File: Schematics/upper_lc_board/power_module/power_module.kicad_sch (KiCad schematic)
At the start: 21 parts, among them U13 ID_LM66100DCKR, U14 ID_LM66100DCKR

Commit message: finish adding components to layout, revise layout next.
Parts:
- C?: value 10uF_16V -> 22uF_16V
- C?: value 47uF_63V -> 100uF_50V
- C?: value 10uF_12V -> 22uF_12V
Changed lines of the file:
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@@
 			)
 		)
-		(property "Value" "10uF_16V"
+		(property "Value" "22uF_16V"
 			(at 57.15 143.5099 0)
 			(effects
@@
 			)
 		)
-		(property "Value" "47uF_63V"
+		(property "Value" "100uF_50V"
 			(at 57.15 167.6399 0)
 			(effects
@@
 			)
 		)
-		(property "Value" "10uF_12V"
+		(property "Value" "22uF_12V"
 			(at 57.15 120.6499 0)
 			(effects

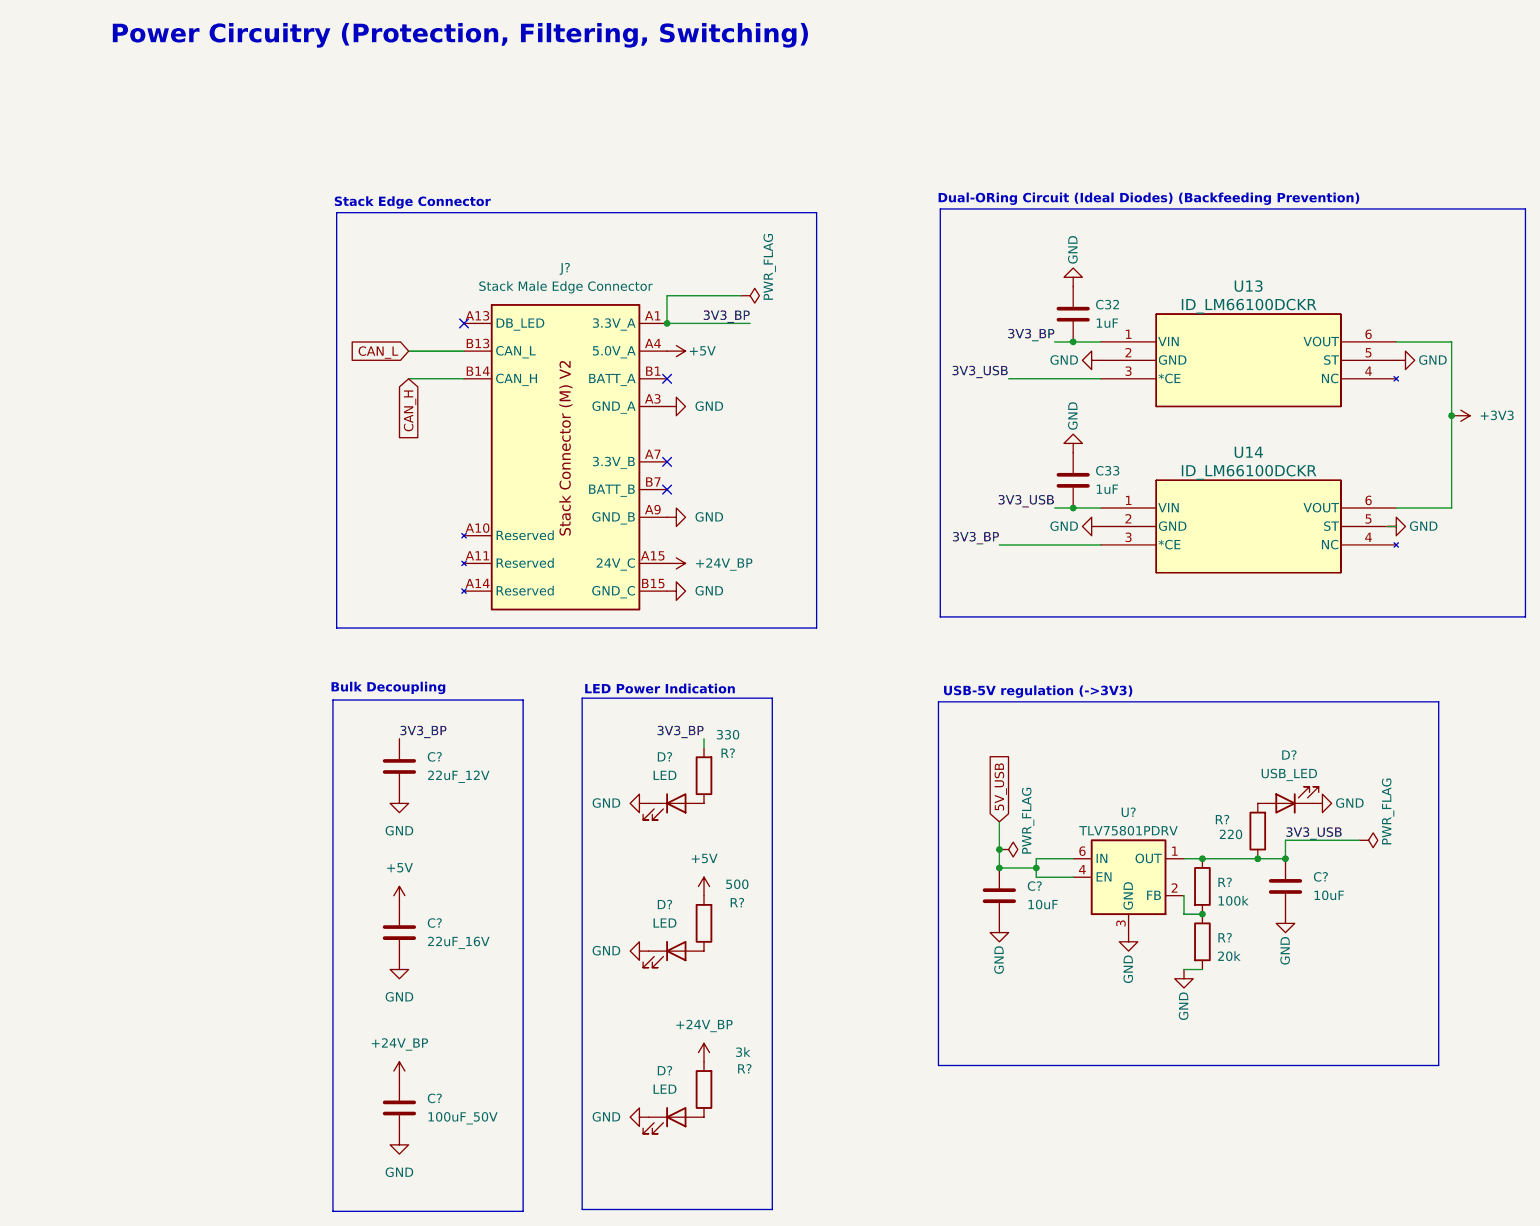
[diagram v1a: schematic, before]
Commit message: add testing points throughout board schematic
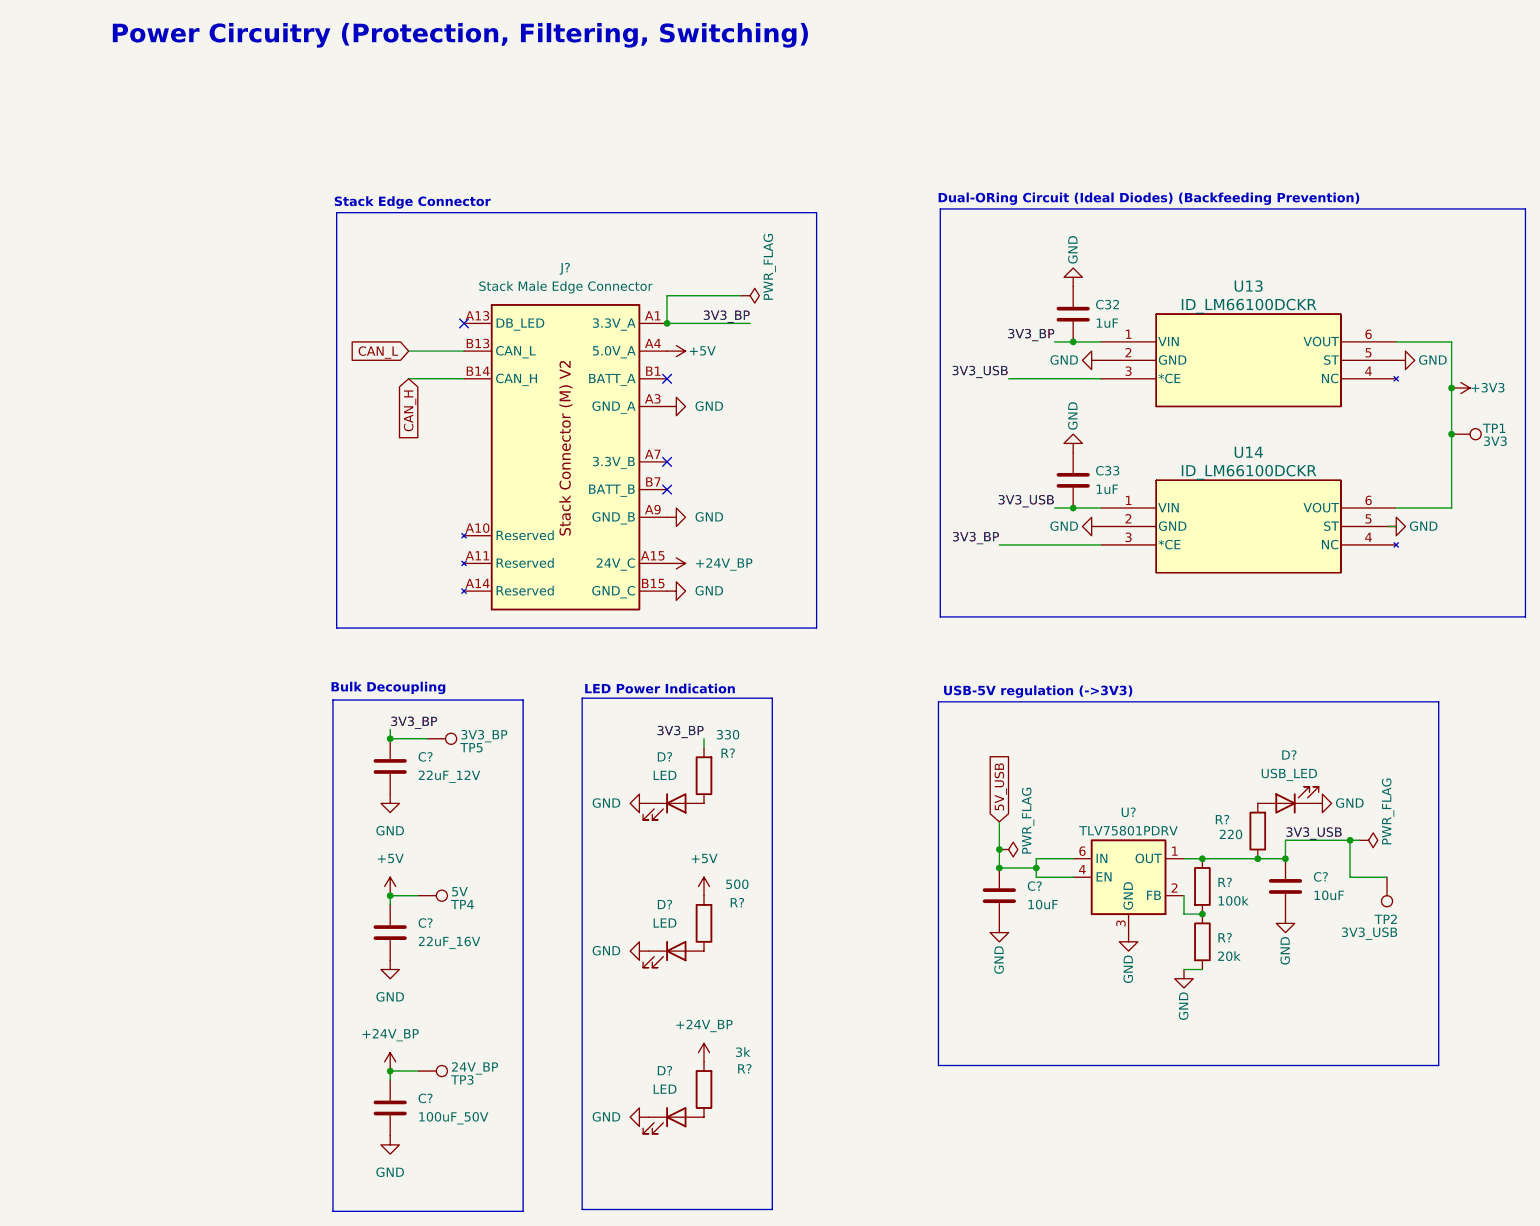
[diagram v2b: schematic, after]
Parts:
- added TP1: 3V3, TestPoint:TestPoint_Pad_1.0x1.0mm, symbol Connector:TestPoint
- added TP2: 3V3_USB, TestPoint:TestPoint_Pad_1.0x1.0mm, symbol Connector:TestPoint
- added TP3: 24V_BP, TestPoint:TestPoint_Pad_1.0x1.0mm, symbol Connector:TestPoint
- added TP4: 5V, TestPoint:TestPoint_Pad_1.0x1.0mm, symbol Connector:TestPoint
- added TP5: 3V3_BP, TestPoint:TestPoint_Pad_1.0x1.0mm, symbol Connector:TestPoint
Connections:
- net +24V_BP: now also TP3.1
- net +3V3: now also TP1.1
- net +5V: now also TP4.1
- net 3V3_BP: now also TP5.1
- net 3V3_USB: now also TP2.1
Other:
- moved on the sheet: C?

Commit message: fix shunt resistor, add test point to layout
- sync issue with backplane connector footprint
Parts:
- TP1, TP2, TP3, TP4, TP5: footprint TestPoint:TestPoint_Pad_1.0x1.0mm -> TestPoint:TestPoint_Pad_D1.0mm
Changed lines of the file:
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@@
 			)
 		)
-		(property "Footprint" "TestPoint:TestPoint_Pad_1.0x1.0mm"
+		(property "Footprint" "TestPoint:TestPoint_Pad_D1.0mm"
 			(at 184.15 134.62 0)
 			(effects
@@
 			)
 		)
-		(property "Footprint" "TestPoint:TestPoint_Pad_1.0x1.0mm"
+		(property "Footprint" "TestPoint:TestPoint_Pad_D1.0mm"
 			(at 57.15 120.65 0)
 			(effects
@@
 			)
 		)
-		(property "Footprint" "TestPoint:TestPoint_Pad_1.0x1.0mm"
+		(property "Footprint" "TestPoint:TestPoint_Pad_D1.0mm"
 			(at 198.12 78.74 0)
 			(effects
@@
 			)
 		)
-		(property "Footprint" "TestPoint:TestPoint_Pad_1.0x1.0mm"
+		(property "Footprint" "TestPoint:TestPoint_Pad_D1.0mm"
 			(at 55.88 142.24 0)
 			(effects
@@
 			)
 		)
-		(property "Footprint" "TestPoint:TestPoint_Pad_1.0x1.0mm"
+		(property "Footprint" "TestPoint:TestPoint_Pad_D1.0mm"
 			(at 55.88 166.37 0)
 			(effects

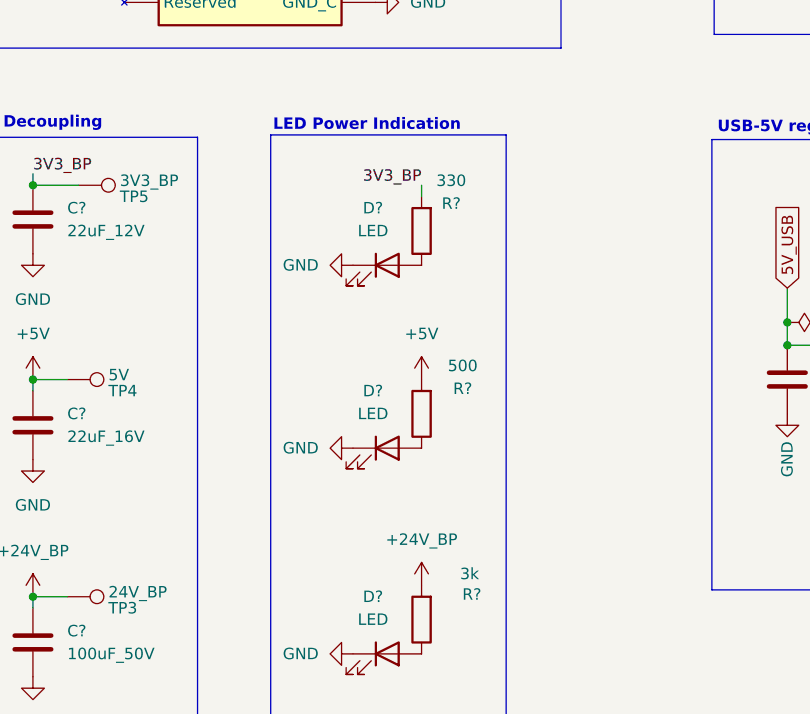
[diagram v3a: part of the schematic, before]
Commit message: start routing
- routing done for solenoids, power, and some other sub-circuits.
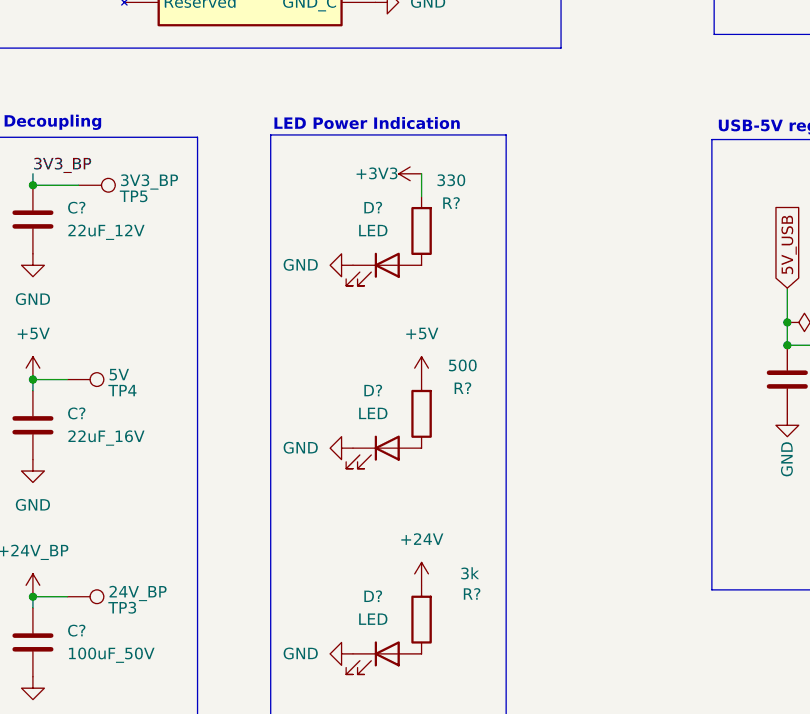
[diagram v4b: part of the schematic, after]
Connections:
- net +24V_BP: no longer R?.2
- net +3V3: now also R?.2
- net 3V3_BP: no longer R?.2
- new net +24V: R?.2
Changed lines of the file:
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@@
 	(wire
 		(pts
-			(xy 95.25 115.57) (xy 95.25 116.84)
-		)
-		(stroke
-			(width 0)
-			(type default)
-			(color 194 0 0 1)
-		)
-	)
-	(wire
-		(pts
 			(xy 143.51 83.82) (xy 146.05 83.82)
 		)
@@
 		)
 	)
+	(wire
+		(pts
+			(xy 95.25 114.3) (xy 95.25 116.84)
+		)
+		(stroke
+			(width 0)
+			(type default)
+			(color 132 0 0 1)
+		)
+	)
 	(rectangle
 		(start 44.704 43.18)
@@
 		)
 	)
-	(label "3V3_BP"
-		(at 95.25 115.57 180)
-		(fields_autoplaced yes)
-		(effects
-			(font
-				(size 1.27 1.27)
-			)
-			(justify right bottom)
-		)
-	)
 	(label "3V3_USB"
 		(at 175.26 129.54 0)
@@
 	)
 	(symbol
-		(lib_id "power:+24V")
-		(at 95.25 160.02 0)
-		(unit 1)
-		(exclude_from_sim no)
-		(in_bom yes)
-		(on_board yes)
-		(dnp no)
-		(fields_autoplaced yes)
-		(property "Reference" "#PWR?"
-			(at 95.25 163.83 0)
-			(effects
-				(font
-					(size 1.27 1.27)
-				)
-				(hide yes)
-			)
-		)
-		(property "Value" "+24V_BP"
-			(at 95.25 154.94 0)
-			(effects
-				(font
-					(size 1.27 1.27)
-				)
-			)
-		)
-		(property "Footprint" ""
-			(at 95.25 160.02 0)
-			(effects
-				(font
-					(size 1.27 1.27)
-				)
-				(hide yes)
-			)
-		)
-		(property "Datasheet" ""
-			(at 95.25 160.02 0)
-			(effects
-				(font
-					(size 1.27 1.27)
-				)
-				(hide yes)
-			)
-		)
-		(property "Description" "Power symbol creates a global label with name \"+24V\""
-			(at 95.25 160.02 0)
-			(effects
-				(font
-					(size 1.27 1.27)
-				)
-				(hide yes)
-			)
-		)
-		(pin "1"
-		)
-		(instances
-			(project "power_module"
-				(path "/056a409d-68dc-4414-8eb2-1cb0ecc0d837"
-					(reference "#PWR?")
-					(unit 1)
-				)
-			)
-			(project "power_module"
-				(path "/9b1a1d2a-fad7-4f10-83f3-1f83e9656c75/4448a9b0-3cba-4e30-89c0-980036e20f76"
-					(reference "#PWR039")
-					(unit 1)
-				)
-			)
-		)
-	)
-	(symbol
 		(lib_id "QRET_Buck_PSU:LM66100DCKR")
 		(at 170.18 63.5 0)
@@
 	)
 	(symbol
+		(lib_id "power:+3V3")
+		(at 95.25 114.3 90)
+		(unit 1)
+		(exclude_from_sim no)
+		(in_bom yes)
+		(on_board yes)
+		(dnp no)
+		(property "Reference" "#PWR041"
+			(at 99.06 114.3 0)
+			(effects
+				(font
+					(size 1.27 1.27)
+				)
+				(hide yes)
+			)
+		)
+		(property "Value" "+3V3"
+			(at 92.71 114.3 90)
+			(effects
+				(font
+					(size 1.27 1.27)
+				)
+				(justify left)
+			)
+		)
+		(property "Footprint" ""
+			(at 95.25 114.3 0)
+			(effects
+				(font
+					(size 1.27 1.27)
+				)
+				(hide yes)
+			)
+		)
+		(property "Datasheet" ""
+			(at 95.25 114.3 0)
+			(effects
+				(font
+					(size 1.27 1.27)
+				)
+				(hide yes)
+			)
+		)
+		(property "Description" "Power symbol creates a global label with name \"+3V3\""
+			(at 95.25 114.3 0)
+			(effects
+				(font
+					(size 1.27 1.27)
+				)
+				(hide yes)
+			)
+		)
+		(pin "1"
+		)
+		(instances
+			(project "upper_lc_board"
+				(path "/9b1a1d2a-fad7-4f10-83f3-1f83e9656c75/4448a9b0-3cba-4e30-89c0-980036e20f76"
+					(reference "#PWR041")
+					(unit 1)
+				)
+			)
+		)
+	)
+	(symbol
 		(lib_id "Device:C")
 		(at 146.05 80.01 180)
@@
 					(unit 1)
 				)
+			)
+		)
+	)
+	(symbol
+		(lib_id "power:+24V")
+		(at 95.25 160.02 0)
+		(unit 1)
+		(exclude_from_sim no)
+		(in_bom yes)
+		(on_board yes)
+		(dnp no)
+		(fields_autoplaced yes)
+		(property "Reference" "#PWR039"
+			(at 95.25 163.83 0)
+			(effects
+				(font
+					(size 1.27 1.27)
+				)
+				(hide yes)
+			)
+		)
+		(property "Value" "+24V"
+			(at 95.25 154.94 0)
+			(effects
+				(font
+					(size 1.27 1.27)
+				)
+			)
+		)
+		(property "Footprint" ""
+			(at 95.25 160.02 0)
+			(effects
+				(font
+					(size 1.27 1.27)
+				)
+				(hide yes)
+			)
+		)
+		(property "Datasheet" ""
+			(at 95.25 160.02 0)
+			(effects
+				(font
+					(size 1.27 1.27)
+				)
+				(hide yes)
+			)
+		)
+		(property "Description" "Power symbol creates a global label with name \"+24V\""
+			(at 95.25 160.02 0)
+			(effects
+				(font
+					(size 1.27 1.27)
+				)
+				(hide yes)
+			)
+		)
+		(pin "1"
+		)
+		(instances
+			(project "upper_lc_board"
+				(path "/9b1a1d2a-fad7-4f10-83f3-1f83e9656c75/4448a9b0-3cba-4e30-89c0-980036e20f76"
+					(reference "#PWR039")
+					(unit 1)
+				)

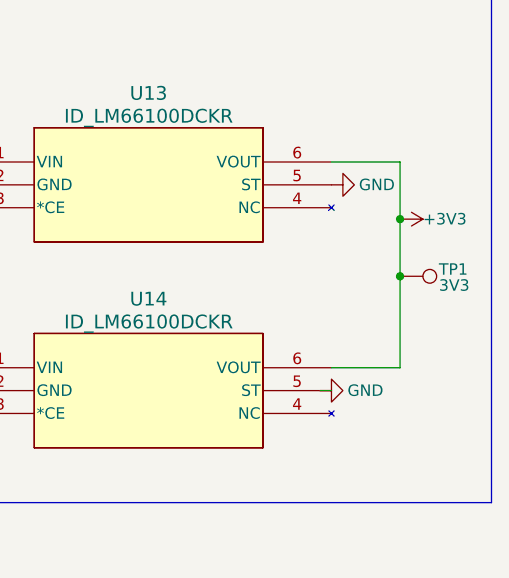
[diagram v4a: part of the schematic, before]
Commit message: more routing work
USB routing
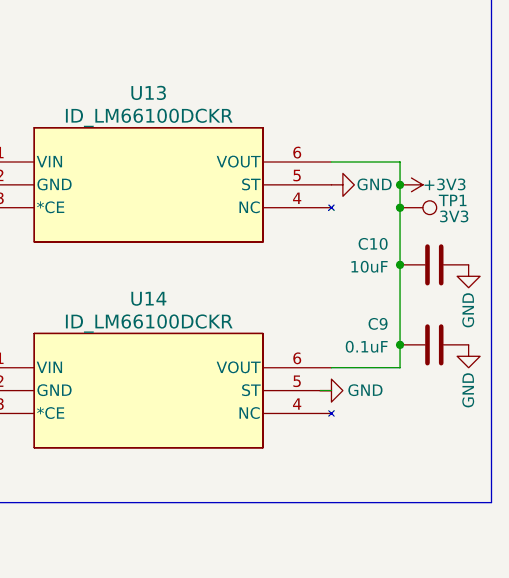
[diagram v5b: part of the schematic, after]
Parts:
- added C10: 10uF, Capacitor_SMD:C_0603_1608Metric, symbol Device:C
- added C9: 0.1uF, Capacitor_SMD:C_0603_1608Metric, symbol Device:C
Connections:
- net +3V3: now also C10.2, C9.2
- net GND: now also C10.1, C9.1
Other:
- moved on the sheet: TP1
